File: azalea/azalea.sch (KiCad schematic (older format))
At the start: 103 parts, among them J1 NEIGHBOR1, J2 NEIGHBOR2, J3 USB-MICRO-B-SHIELDED, J4 USB-MICRO-B-SHIELDED, J5 JTAG, J6 POWER, J7 BONUS_ROW, SW1 DFU, SW2 RESET, U1 LPC4330FBD144, U2 W25Q16DV, U3 AP7333, U4 IP4220CZ6, U5 AP2553W6-7, X1 MCU_XTAL, X2 RTC_XTAL

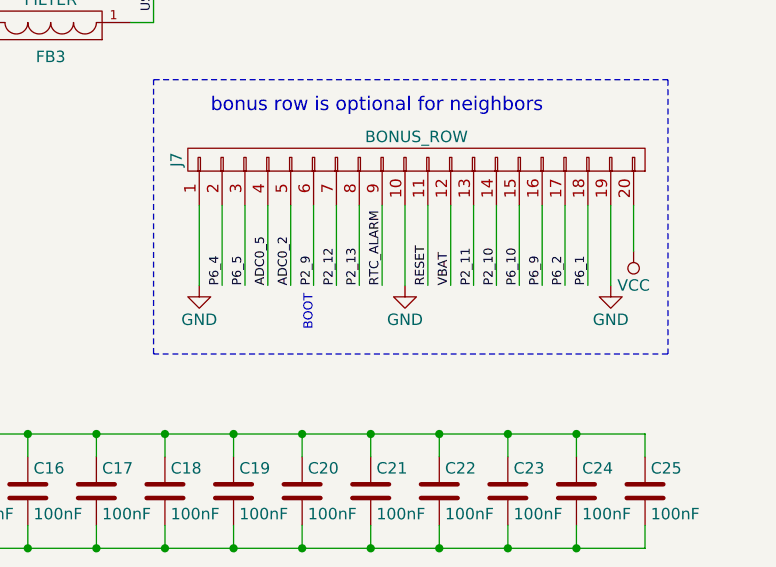
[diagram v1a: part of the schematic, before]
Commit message: Azalea: changed J7 pin 10 from GND to RTCX1
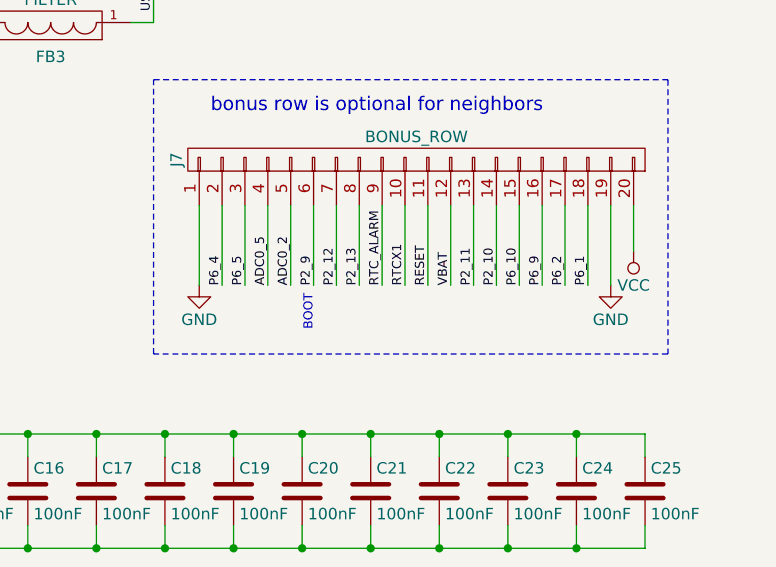
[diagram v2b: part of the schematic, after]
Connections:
- net GND: no longer J7.10 (P10)
- net RTCX1: now also J7.10 (P10)
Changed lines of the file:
@@
 LIBS:valves
 LIBS:gsg-symbols
-LIBS:greatfet-one-cache
+LIBS:azalea-cache
 EELAYER 25 0
 EELAYER END
@@
 Comp "Copyright 2015-2018 Great Scott Gadgets"
 Comment1 "License: BSD-3-Clause"
-Comment2 "http://greatscottgadgets.com/greatfet/"
+Comment2 "https://greatscottgadgets.com/greatfet/"
 Comment3 ""
 Comment4 ""
@@
 	1    0    0    -1
 $EndComp
-$Comp
-L GND #PWR082
-U 1 1 56036BE7
-P 15150 7550
-F 0 "#PWR082" H 15150 7300 50  0001 C CNN
-F 1 "GND" H 15150 7400 50  0000 C CNN
-F 2 "" H 15150 7550 60  0000 C CNN
-F 3 "" H 15150 7550 60  0000 C CNN
-	1    15150 7550
-	1    0    0    -1
-$EndComp
 Text Label 3850 5100 0    40   ~ 0
 USB0_D+
@@
 Text Notes 5150 2000 0    60   ~ 0
 pin straps for hardware\nversion detection
+Text Label 15150 7550 1    40   ~ 0
+RTCX1
 $EndSCHEMATC
